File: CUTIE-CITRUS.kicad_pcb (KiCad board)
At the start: 2 copper layers, 19 parts, among them U7 ASEK-32.768KHZ-L-R-T, U8 AP3441SHE-7B

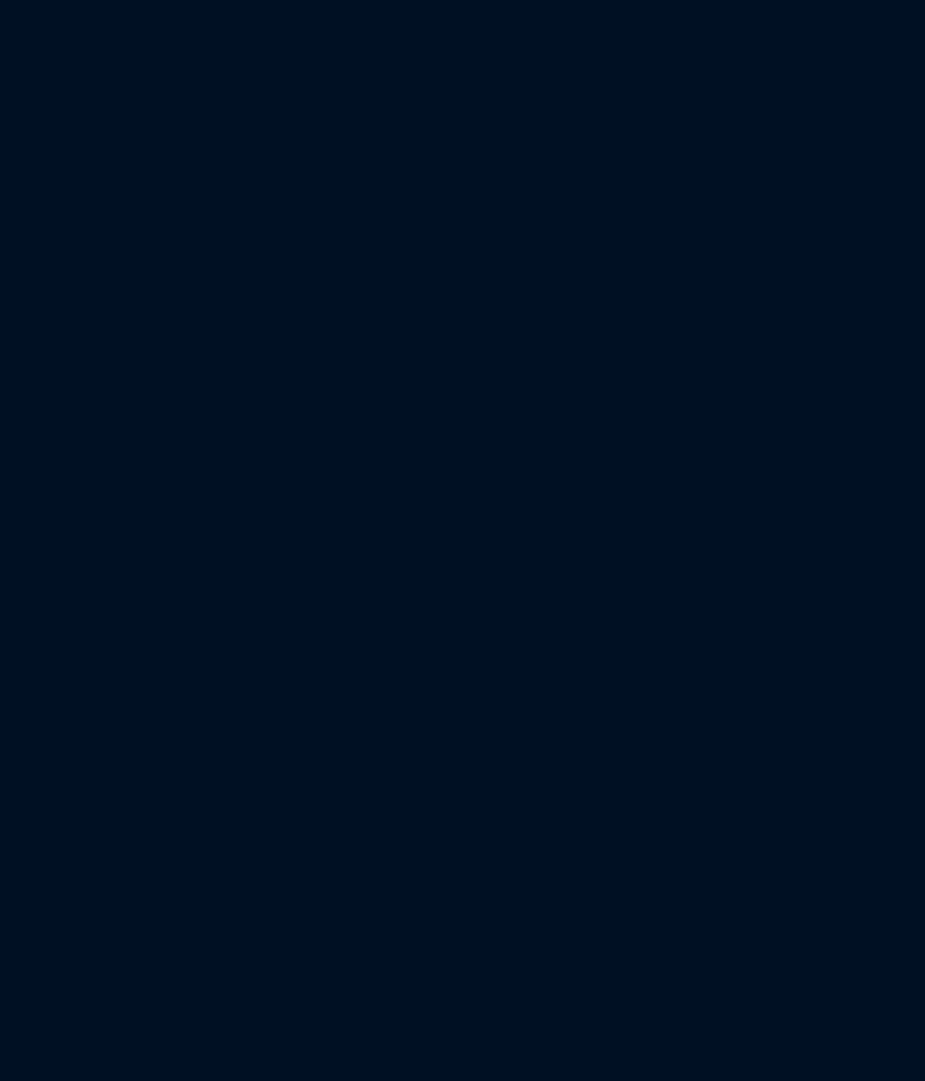
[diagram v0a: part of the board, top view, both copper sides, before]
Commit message: restructured symbols, added footprints
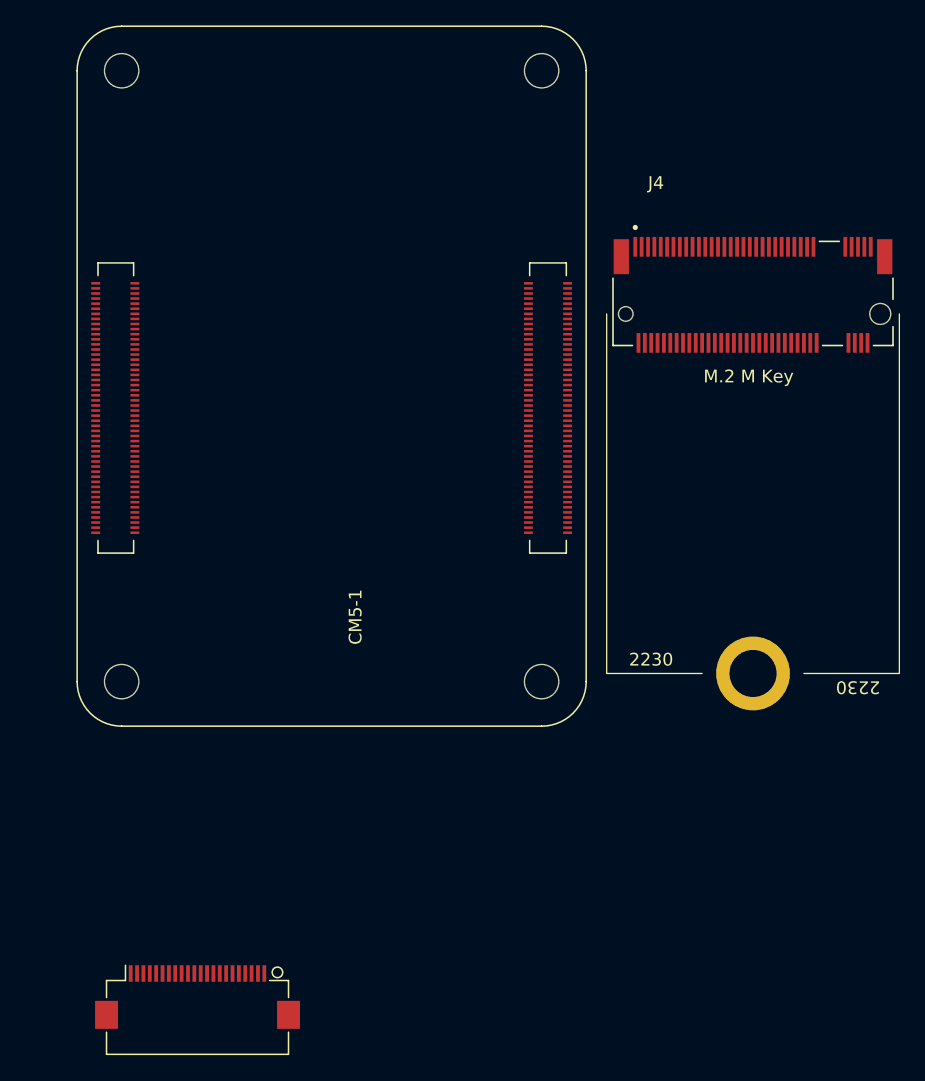
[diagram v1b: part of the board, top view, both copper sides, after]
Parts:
- added CM5-1: 2x 10164227-1001A1RLF, library:RPi-CM5, F.Cu at (153.9, 100.3)
- added J2: F32Q-1A7H1-11022, library:Hirose_FH12-22S-0.5SH_1x22-1MP_P0.50mm_Horizontal, F.Cu at (159.8, 125.1)
- added J4: Bus_M.2_Socket_M, library:2230m2, F.Cu at (203.5, 71.4)
- C10, C19: value 100n -> 100nF
- C14, C15, C16, C17, C4, C6: value 10u -> 10uF
- R17: value 1k -> 1K
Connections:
- net /NVME/+5v renamed /CM5 Connectors/5V0
- net /NVME/M2_3v3 renamed /NVME/3V3_M2
- net /NVME/PCIE_PWR_EN renamed /CM5 Connectors/PCIE_PWR_EN
- net Net-(U8-LX) renamed /NVME/LX
- D1 pad 2: /CM5 Connectors/+3.3v -> /CM5 Connectors/3V3
- R17 pad 2: unconnected-(R17-Pad2) -> /NVME/nLED1
- U7 pad 3: unconnected-(U7-Out-Pad3) -> /NVME/SUSCLK

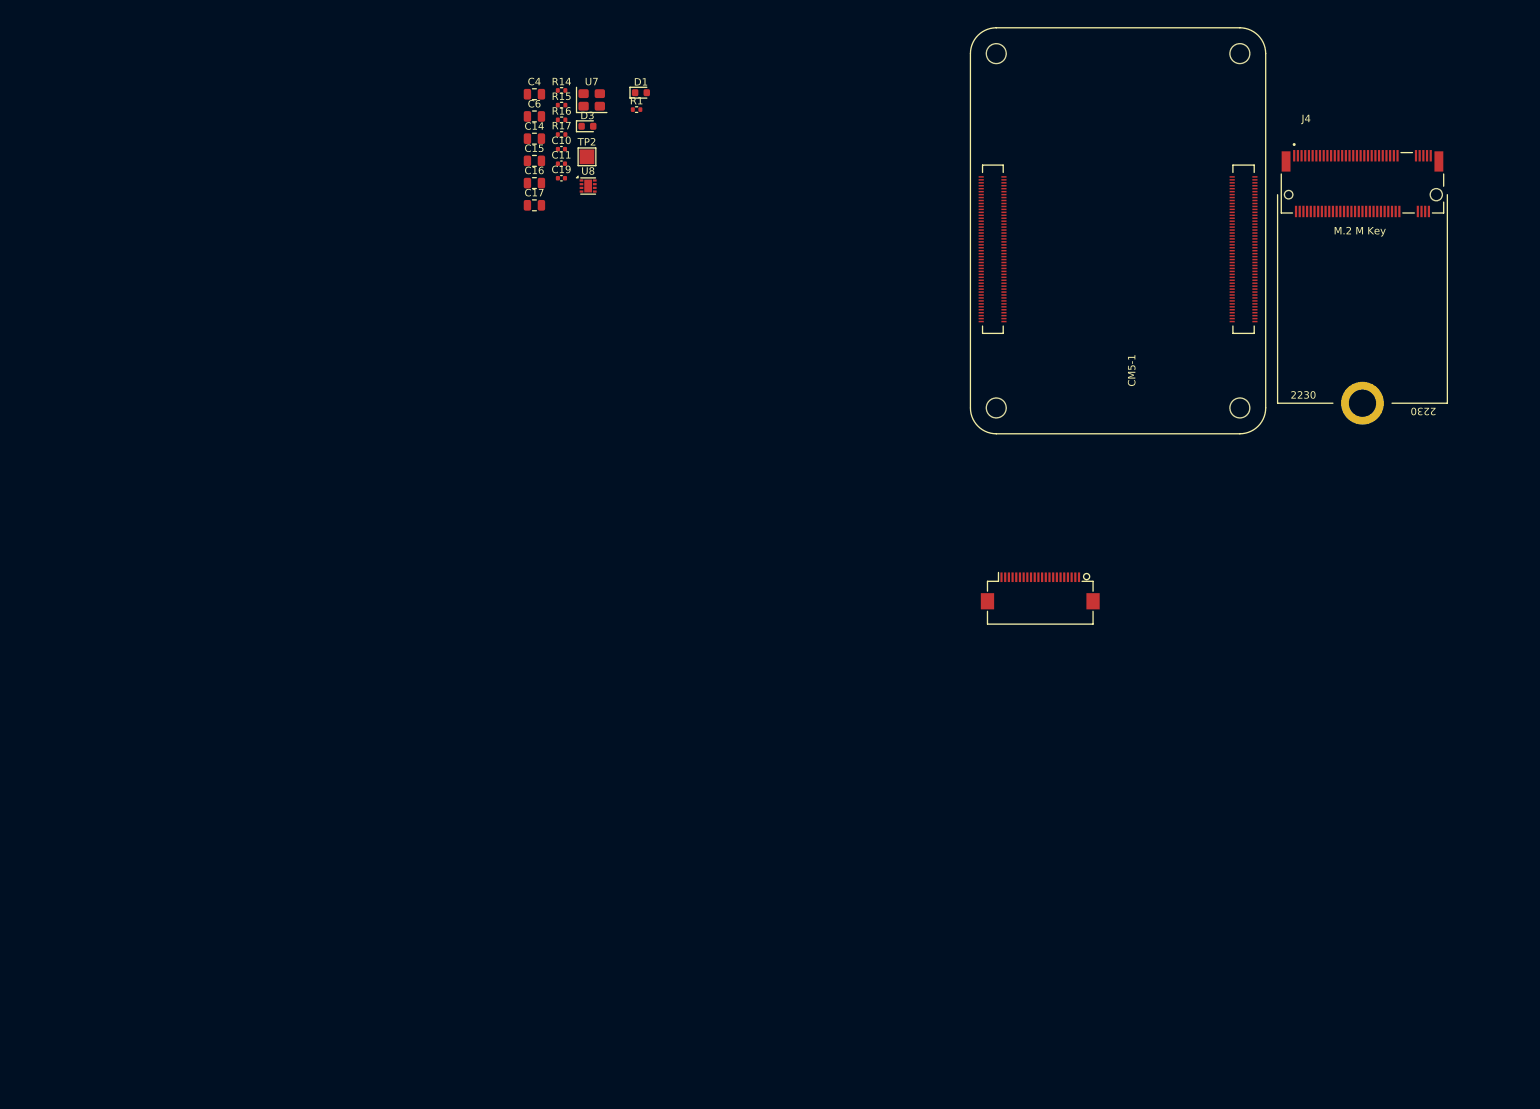
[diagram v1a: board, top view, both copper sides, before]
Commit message: extra abstraction layer for cm5 conns.
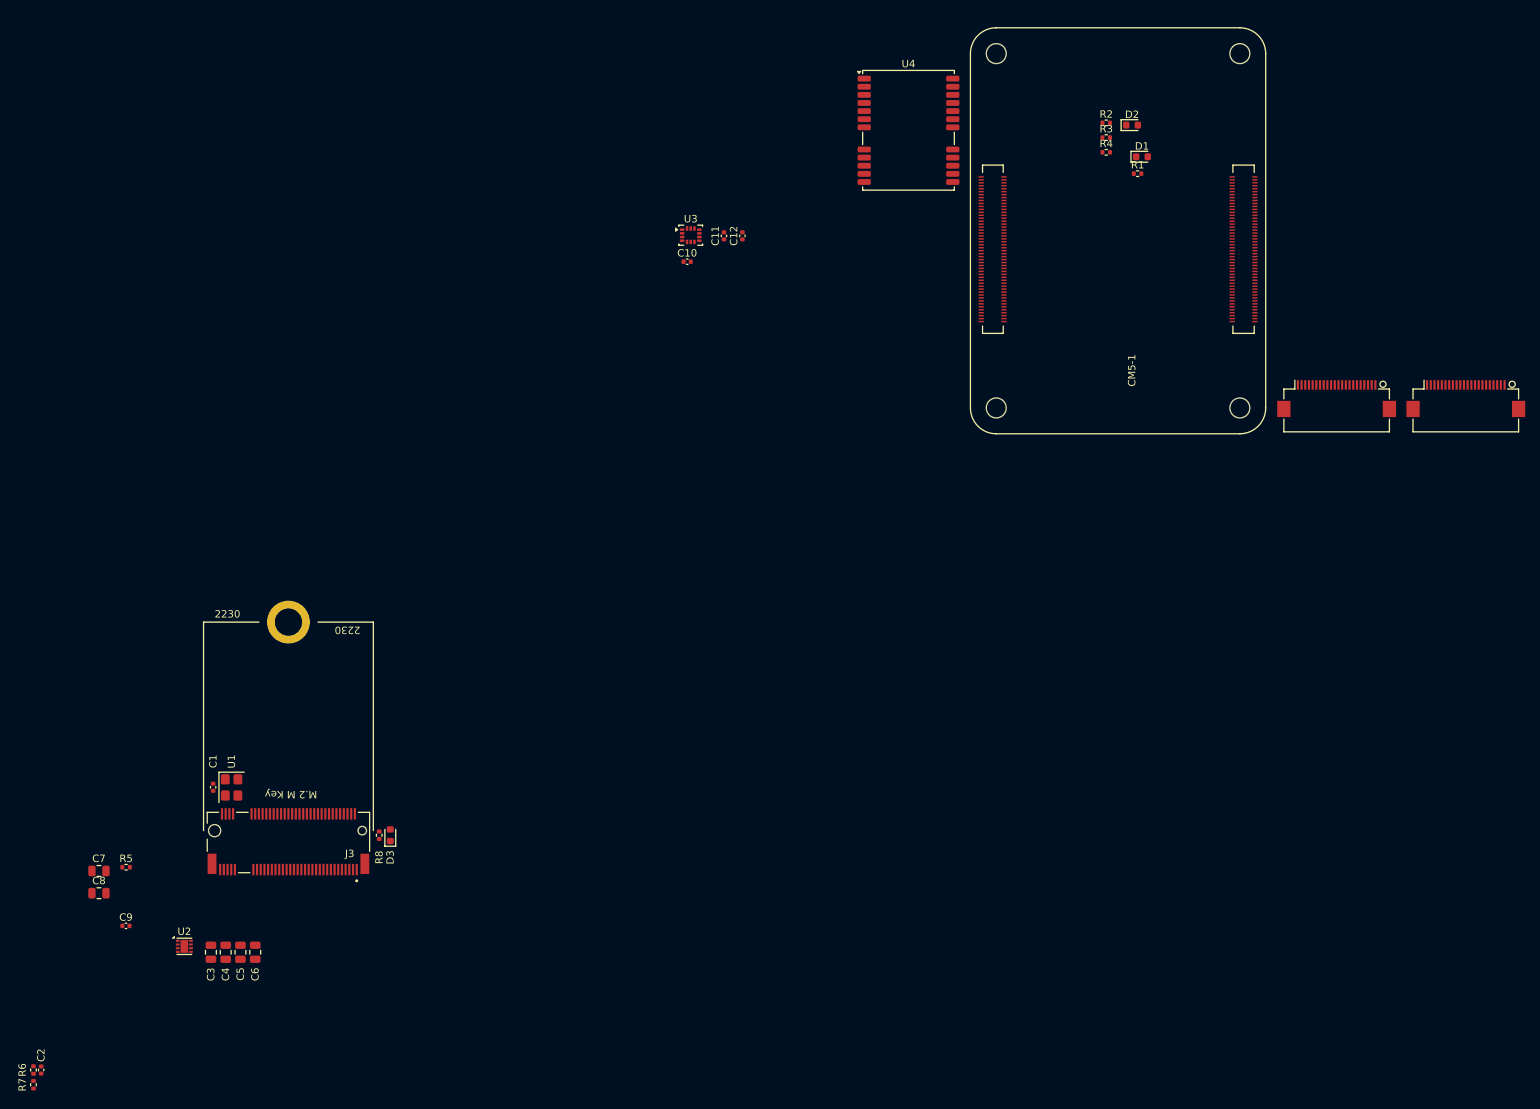
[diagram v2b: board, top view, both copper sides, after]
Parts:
- removed TP2: TestPoint, TestPoint:TestPoint_Pad_2.0x2.0mm
- added C10: 10nF, Capacitor_SMD:C_0402_1005Metric, F.Cu at (112.0, 80.5)
- added C11: 0.1uF, Capacitor_SMD:C_0402_1005Metric, F.Cu at (117.0, 77.0)
- added C12: 2.2uF, Capacitor_SMD:C_0402_1005Metric, F.Cu at (119.5, 77.0)
- added D2: LED Red, LED_SMD:LED_0603_1608Metric, F.Cu at (172.3, 62.0)
- added J2: F32Q-1A7H1-11022, library:Hirose_FH12-22S-0.5SH_1x22-1MP_P0.50mm_Horizontal, F.Cu at (200.0, 99.0)
- added R2: 2.2K 1%, Resistor_SMD:R_0402_1005Metric, F.Cu at (168.8, 61.7)
- added R3: 2.2K 1%, Resistor_SMD:R_0402_1005Metric, F.Cu at (168.8, 63.7)
- added R4: 1k, Resistor_SMD:R_0402_1005Metric, F.Cu at (168.8, 65.7)
- added U3: ICM-42688-P, Package_LGA:LGA-14_3x2.5mm_P0.5mm_LayoutBorder3x4y, F.Cu at (112.5, 76.9)
- added U4: NEO-M8M, RF_GPS:ublox_NEO, F.Cu at (142.0, 62.7)
- C1: renamed from C19; value 100nF -> 0.1uF
- C9: renamed from C10; value 100nF -> 0.1uF
- moved J3 169.1 mm to (58.0, 157.6), turned to 180 degrees
- moved R7 149.0 mm to (23.5, 192.0), turned to -90 degrees
- moved R6 149.0 mm to (23.5, 190.0), turned to -90 degrees
- moved C2 141.6 mm to (24.5, 190.0), turned to -90 degrees
- moved C8 120.6 mm to (32.3, 166.1)
- moved C7 120.6 mm to (32.3, 163.0)
- moved C9 120.6 mm to (36.0, 170.5)
- moved R5 120.6 mm to (36.0, 162.5)
- moved C3 118.6 mm to (47.5, 174.1), turned to -90 degrees
- moved U2 116.6 mm to (43.9, 173.2)
- moved C4 115.1 mm to (49.5, 174.1), turned to -90 degrees
- moved C5 111.5 mm to (51.5, 174.1), turned to -90 degrees
- moved C6 108.0 mm to (53.5, 174.1), turned to -90 degrees
- moved U1 105.1 mm to (50.3, 151.7), turned to -90 degrees
- moved D3 99.7 mm to (71.8, 158.2), turned to 90 degrees
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- renumbered C11 to C2, C14 to C3, C15 to C4, C16 to C5, C17 to C6, C4 to C7, C6 to C8, J2 to J1, J4 to J3, R14 to R5, R15 to R6, R16 to R7, R17 to R8, U7 to U1, U8 to U2
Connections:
- net /CM5 Connectors/5V0 renamed /CM5/5V0
- net /CM5 Connectors/CAM_GPIO0 renamed /CM5/CAM_GPIO0
- net /CM5 Connectors/DPHY0.C_N renamed /CM5/DPHY0.C_N
- net /CM5 Connectors/DPHY0.C_P renamed /CM5/DPHY0.C_P
- net /CM5 Connectors/DPHY0.D0_N renamed /CM5/DPHY0.D0_N
- net /CM5 Connectors/DPHY0.D0_P renamed /CM5/DPHY0.D0_P
- net /CM5 Connectors/DPHY0.D1_N renamed /CM5/DPHY0.D1_N
- net /CM5 Connectors/DPHY0.D1_P renamed /CM5/DPHY0.D1_P
- net /CM5 Connectors/DPHY0.D2_N renamed /CM5/DPHY0.D2_N
- net /CM5 Connectors/DPHY0.D2_P renamed /CM5/DPHY0.D2_P
- net /CM5 Connectors/DPHY0.D3_N renamed /CM5/DPHY0.D3_N
- net /CM5 Connectors/DPHY0.D3_P renamed /CM5/DPHY0.D3_P
- net /CM5 Connectors/PCIE.CLK_N renamed /CM5/PCIE.CLK_N
- net /CM5 Connectors/PCIE.CLK_P renamed /CM5/PCIE.CLK_P
- net /CM5 Connectors/PCIE.RX_N renamed /CM5/PCIE.RX_N
- net /CM5 Connectors/PCIE.RX_P renamed /CM5/PCIE.RX_P
- net /CM5 Connectors/PCIE.TX_N renamed /CM5/PCIE.TX_N
- net /CM5 Connectors/PCIE.TX_P renamed /CM5/PCIE.TX_P
- net /CM5 Connectors/PCIE_PWR_EN renamed /CM5/PCIE_PWR_EN
- net /CM5 Connectors/PCIE_nCLKREQ renamed /CM5/PCIE_nCLKREQ
- net /CM5 Connectors/PCIE_nRST renamed /CM5/PCIE_nRST
- net /CM5 Connectors/PCIE_nWAKE renamed /CM5/PCIE_nWAKE
- net /CM5 Connectors/VBUS_EN renamed /CM5/VBUS_EN
- CM5-1 pad 175: unconnected-(CM5-1B-MIPI1_D0_N-Pad175) -> /CM5/DPHY1.D0_N
- CM5-1 pad 177: unconnected-(CM5-1B-MIPI1_D0_P-Pad177) -> /CM5/DPHY1.D0_P
- CM5-1 pad 181: unconnected-(CM5-1B-MIPI1_D1_N-Pad181) -> /CM5/DPHY1.D1_N
- CM5-1 pad 183: unconnected-(CM5-1B-MIPI1_D1_P-Pad183) -> /CM5/DPHY1.D1_P
- CM5-1 pad 187: unconnected-(CM5-1B-MIPI1_C_N-Pad187) -> /CM5/DPHY1.C_N
- CM5-1 pad 189: unconnected-(CM5-1B-MIPI1_C_P-Pad189) -> /CM5/DPHY1.C_P
- CM5-1 pad 193: unconnected-(CM5-1B-MIPI1_D2_N-Pad193) -> /CM5/DPHY1.D2_N
- CM5-1 pad 194: unconnected-(CM5-1B-MIPI1_D3_N-Pad194) -> /CM5/DPHY1.D3_N
- CM5-1 pad 195: unconnected-(CM5-1B-MIPI1_D2_P-Pad195) -> /CM5/DPHY1.D2_P
- CM5-1 pad 196: unconnected-(CM5-1B-MIPI1_D3_P-Pad196) -> /CM5/DPHY1.D3_P
- CM5-1 pad 35: unconnected-(CM5-1A-ID_SC-Pad35) -> /CM5/I2C1.SCL
- CM5-1 pad 36: unconnected-(CM5-1A-ID_SD-Pad36) -> /CM5/I2C1.SDA
- CM5-1 pad 37: unconnected-(CM5-1A-GPIO7-Pad37) -> /CM5/SPI0.CS1n
- CM5-1 pad 38: unconnected-(CM5-1A-GPIO11-Pad38) -> /CM5/SPI0.SCLK
- CM5-1 pad 39: unconnected-(CM5-1A-GPIO8-Pad39) -> /CM5/SPI0.CS0n
- CM5-1 pad 40: unconnected-(CM5-1A-GPIO9-Pad40) -> /CM5/SPI0.MISO
- CM5-1 pad 44: unconnected-(CM5-1A-GPIO10-Pad44) -> /CM5/SPI0.MOSI
- CM5-1 pad 78: unconnected-(CM5-1A-GPIO_VREF(1.8v/3.3v_Input)-Pad78) -> /CM5/3V3
- CM5-1 pad 84: /CM5 Connectors/3V3 -> /CM5/3V3
- CM5-1 pad 86: /CM5 Connectors/3V3 -> /CM5/3V3
- CM5-1 pad 88: /CM5 Connectors/1V8 -> unconnected-(CM5-1A-+1.8v_(Output)-Pad88)
- CM5-1 pad 90: /CM5 Connectors/1V8 -> unconnected-(CM5-1A-+1.8v_(Output)-Pad90)
- CM5-1 pad 93: unconnected-(CM5-1A-nRPIBOOT-Pad93) -> GND
- CM5-1 pad 95: unconnected-(CM5-1A-LED_nPWR-Pad95) -> Net-(CM5-1A-LED_nPWR)
- D1 pad 2: /CM5 Connectors/3V3 -> /CM5/3V3
- J1 pad 20: GND -> /CM5/I2C0.SCL
- J1 pad 21: GND -> /CM5/I2C0.SDA
- J1 pad 22: /CM5 Connectors/3V3 -> /CM5/3V3

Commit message: neo m8m impl.
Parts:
- added 3V3: TestPoint, TestPoint:TestPoint_Pad_D1.0mm, F.Cu at (136.3, 110.5)
- added 5V0: TestPoint, TestPoint:TestPoint_Pad_D1.0mm, F.Cu at (136.3, 113.6)
- added D4: TPD1E05U06DPY, Package_SON:Texas_DPY0002A_0.6x1mm_P0.65mm, F.Cu at (178.7, 109.0)
- added J4: Hirose U.FL, Connector_Coaxial:U.FL_Hirose_U.FL-R-SMT-1_Vertical, F.Cu at (179.7, 95.0)
- added TP1: TestPoint, TestPoint:TestPoint_Pad_D1.0mm, F.Cu at (136.3, 116.6)
- added TP10: TestPoint, TestPoint:TestPoint_Pad_D1.0mm, F.Cu at (145.5, 116.6)
- added TP11: TestPoint, TestPoint:TestPoint_Pad_D1.0mm, F.Cu at (148.5, 110.5)
- added TP12: TestPoint, TestPoint:TestPoint_Pad_D1.0mm, F.Cu at (148.5, 113.6)
- added TP13: TestPoint, TestPoint:TestPoint_Pad_D1.0mm, F.Cu at (148.5, 116.6)
- added TP2: TestPoint, TestPoint:TestPoint_Pad_D1.0mm, F.Cu at (139.4, 110.5)
- added TP3: TestPoint, TestPoint:TestPoint_Pad_D1.0mm, F.Cu at (139.4, 113.6)
- added TP4: TestPoint, TestPoint:TestPoint_Pad_D1.0mm, F.Cu at (139.4, 116.6)
- added TP5: TestPoint, TestPoint:TestPoint_Pad_D1.0mm, F.Cu at (142.4, 110.5)
- added TP6: TestPoint, TestPoint:TestPoint_Pad_D1.0mm, F.Cu at (142.4, 113.6)
- added TP7: TestPoint, TestPoint:TestPoint_Pad_D1.0mm, F.Cu at (142.4, 116.6)
- added TP8: TestPoint, TestPoint:TestPoint_Pad_D1.0mm, F.Cu at (145.5, 110.5)
- added TP9: TestPoint, TestPoint:TestPoint_Pad_D1.0mm, F.Cu at (145.5, 113.6)
- moved C2 203.6 mm to (190.3, 71.9), turned to 0 degrees
- moved R7 202.0 mm to (187.4, 73.9), turned to 0 degrees
- moved R6 202.0 mm to (187.4, 71.9), turned to 0 degrees
- moved C3 186.0 mm to (188.2, 52.4), turned to 0 degrees
- moved C7 184.4 mm to (188.2, 64.4)
- moved C8 184.4 mm to (188.2, 67.4)
- moved C4 182.5 mm to (188.2, 55.4), turned to 0 degrees
- moved C9 182.1 mm to (190.3, 73.9)
- moved C5 179.0 mm to (188.2, 58.4), turned to 0 degrees
- moved R5 177.5 mm to (187.4, 69.9)
- moved C6 175.6 mm to (188.2, 61.4), turned to 0 degrees
- moved U2 169.9 mm to (188.1, 83.4)
- moved C1 164.3 mm to (190.3, 69.9), turned to 0 degrees
- moved U1 156.1 mm to (188.6, 79.2), turned to 0 degrees
- moved J3 152.6 mm to (173.9, 58.4), turned to 0 degrees
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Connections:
- net /CM5/5V0 renamed /NVME/5V0
- net /CM5/I2C0.SCL renamed /Cameras/I2C0.SCL
- net /CM5/I2C0.SDA renamed /Cameras/I2C0.SDA
- net /CM5/PCIE_PWR_EN renamed /CM5/PCIEsb.PWR_EN
- net /CM5/PCIE_nCLKREQ renamed /CM5/PCIEsb.nCLKREQ
- net /CM5/PCIE_nRST renamed /CM5/PCIEsb.nRST
- net /CM5/PCIE_nWAKE renamed /CM5/PCIEsb.nWAKE
- net /CM5/VBUS_EN renamed /CM5/High-Speed Serial/VBUS_EN
- C10 pad 1: /CM5/3V3 -> /Cameras/3V3
- C11 pad 1: /CM5/3V3 -> /Cameras/3V3
- C12 pad 1: /CM5/3V3 -> /Cameras/3V3
- CM5-1 pad 100: GND -> /CM5/CAM_GPIO1
- CM5-1 pad 78: /CM5/3V3 -> /Cameras/3V3
- CM5-1 pad 80: GND -> /CM5/GPIO/I2C0.SCL
- CM5-1 pad 82: GND -> /CM5/GPIO/I2C0.SDA
- CM5-1 pad 84: /CM5/3V3 -> /Cameras/3V3
- CM5-1 pad 86: /CM5/3V3 -> /Cameras/3V3
- D1 pad 2: /CM5/3V3 -> /Cameras/3V3
- D2 pad 2: /CM5/3V3 -> /Cameras/3V3
- J1 pad 18: GND -> /CM5/CAM_GPIO1
- J1 pad 22: /CM5/3V3 -> /Cameras/3V3
- J2 pad 22: /CM5/3V3 -> /Cameras/3V3
- R2 pad 1: /CM5/3V3 -> /Cameras/3V3
- R3 pad 1: /CM5/3V3 -> /Cameras/3V3
- U3 pad 5: /CM5/3V3 -> /Cameras/3V3
- U3 pad 8: /CM5/3V3 -> /Cameras/3V3
- U4 pad 10: Net-(U4-GND-Pad10) -> GND
- U4 pad 11: unconnected-(U4-RF_IN-Pad11) -> Net-(U4-RF_IN)
- U4 pad 12: Net-(U4-GND-Pad10) -> Net-(U4-GND-Pad12)
- U4 pad 13: Net-(U4-GND-Pad10) -> Net-(U4-GND-Pad12)
- U4 pad 18: unconnected-(U4-SDA/~{SPI_CS}-Pad18) -> /CM5/SPI0.CS1n
- U4 pad 19: unconnected-(U4-SCL/SPI_CLK-Pad19) -> /CM5/SPI0.SCLK
- U4 pad 20: unconnected-(U4-TXD/SPI_MISO-Pad20) -> /CM5/SPI0.MISO
- U4 pad 21: unconnected-(U4-RXD/SPI_MOSI-Pad21) -> /CM5/SPI0.MOSI
- U4 pad 22: unconnected-(U4-V_BCKP-Pad22) -> /Cameras/3V3
- U4 pad 23: unconnected-(U4-VCC-Pad23) -> /Cameras/3V3
- U4 pad 24: Net-(U4-GND-Pad10) -> Net-(U4-GND-Pad12)
- U4 pad 7: unconnected-(U4-VDD_USB-Pad7) -> GND
